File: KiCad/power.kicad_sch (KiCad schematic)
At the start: 15 parts

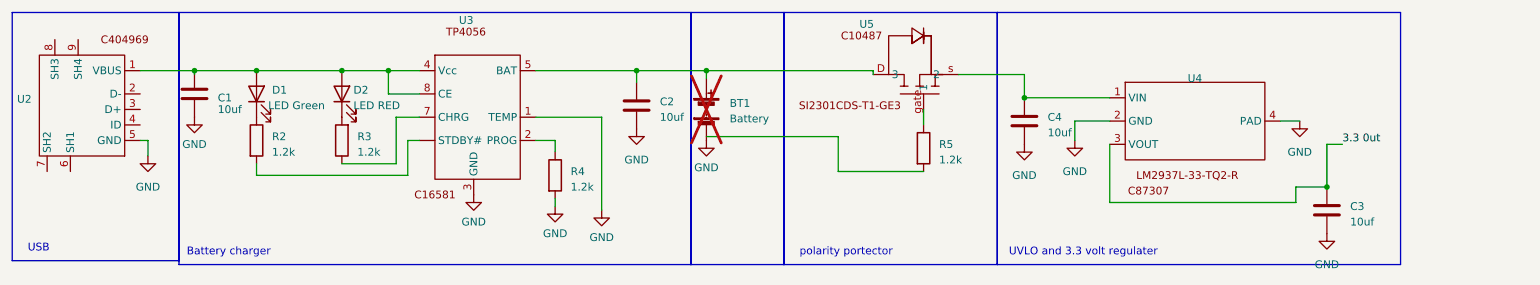
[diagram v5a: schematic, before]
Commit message: added heirachals and connected subsheets
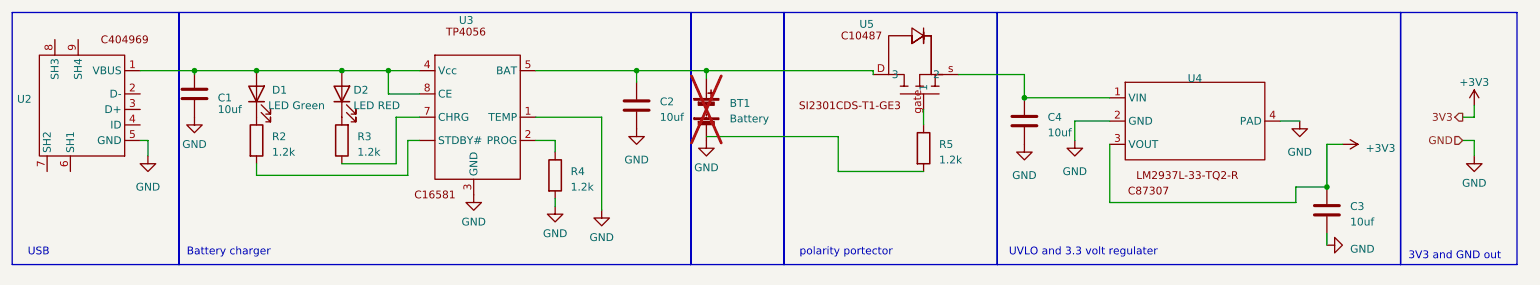
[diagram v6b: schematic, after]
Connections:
- net 3.3 0ut renamed +3V3
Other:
- note added: "3V3 and GND out"
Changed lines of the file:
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@@
+    (stroke (width 0) (type default))
+  )
+  (wire (pts (xy 262.89 38.1) (xy 260.985 38.1))
     (stroke (width 0) (type default))
   )
@@
     (stroke (width 0) (type default))
   )
+  (wire (pts (xy 262.89 36.195) (xy 262.89 38.1))
+    (stroke (width 0) (type default))
+  )
   (wire (pts (xy 189.23 31.115) (xy 189.23 34.925))
     (stroke (width 0) (type default))
@@
     (stroke (width 0) (type default))
   )
+  (wire (pts (xy 260.985 41.91) (xy 262.89 41.91))
+    (stroke (width 0) (type default))
+  )
+  (wire (pts (xy 262.89 41.91) (xy 262.89 44.45))
+    (stroke (width 0) (type default))
+  )
   (wire (pts (xy 63.5 30.48) (xy 77.47 30.48))
     (stroke (width 0) (type default))
@@
     (stroke (width 0) (type default))
   )
+  (wire (pts (xy 238.76 57.15) (xy 238.76 59.055))
+    (stroke (width 0) (type default))
+  )
   (wire (pts (xy 86.36 45.72) (xy 86.36 38.1))
     (stroke (width 0) (type default))
@@
     (fill (type none))
   )
-  (rectangle (start 23.495 20.955) (end 50.8 61.595)
+  (rectangle (start 23.495 20.955) (end 50.8 62.23)
+    (stroke (width 0) (type default))
+    (fill (type none))
+  )
+  (rectangle (start 250.825 20.955) (end 269.875 62.23)
     (stroke (width 0) (type default))
     (fill (type none))
@@
     (effects (font (size 1.27 1.27)) (justify left bottom))
   )
+  (text "3V3 and GND out\n" (at 252.095 61.595 0)
+    (effects (font (size 1.27 1.27)) (justify left bottom))
+  )
   (text "Battery charger " (at 52.07 60.96 0)
     (effects (font (size 1.27 1.27)) (justify left bottom))
   )
-  (text "USB" (at 26.035 60.325 0)
+  (text "USB" (at 26.035 60.96 0)
     (effects (font (size 1.27 1.27)) (justify left bottom))
   )
@@
     (effects (font (size 1.27 1.27)) (justify left bottom))
   )
-  (label "3.3 0ut" (at 241.3 42.545 0) (fields_autoplaced)
-    (effects (font (size 1.27 1.27)) (justify left bottom))
+  (hierarchical_label "GND" (shape input) (at 260.985 41.91 180) (fields_autoplaced)
+    (effects (font (size 1.27 1.27)) (justify right))
+  )
+  (hierarchical_label "3V3" (shape output) (at 260.985 38.1 180) (fields_autoplaced)
+    (effects (font (size 1.27 1.27)) (justify right))
+  )
+  (symbol (lib_id "power:+3V3") (at 241.3 42.545 270) (unit 1)
+    (in_bom yes) (on_board yes) (dnp no) (fields_autoplaced)
+    (property "Reference" "#PWR040" (at 237.49 42.545 0)
+      (effects (font (size 1.27 1.27)) hide)
+    )
+    (property "Value" "+3V3" (at 245.11 43.18 90)
+      (effects (font (size 1.27 1.27)) (justify left))
+    )
+    (property "Footprint" "" (at 241.3 42.545 0)
+      (effects (font (size 1.27 1.27)) hide)
+    )
+    (property "Datasheet" "" (at 241.3 42.545 0)
+      (effects (font (size 1.27 1.27)) hide)
+    )
+    (pin "1")
+    (instances
+      (project "EEE3088F_CKR"
+        (path "/31e5d740-f3fb-4029-be8d-dfdc4f653d72/d53a003e-af2e-46c6-8ee9-c5701cef8adb"
+          (reference "#PWR040") (unit 1)
+        )
+      )
+    )
   )
   (symbol (lib_id "Device:LED") (at 77.47 34.29 90) (unit 1)
@@
     )
   )
+  (symbol (lib_id "power:+3V3") (at 262.89 36.195 0) (unit 1)
+    (in_bom yes) (on_board yes) (dnp no) (fields_autoplaced)
+    (property "Reference" "#PWR041" (at 262.89 40.005 0)
+      (effects (font (size 1.27 1.27)) hide)
+    )
+    (property "Value" "+3V3" (at 262.89 32.385 0)
+      (effects (font (size 1.27 1.27)))
+    )
+    (property "Footprint" "" (at 262.89 36.195 0)
+      (effects (font (size 1.27 1.27)) hide)
+    )
+    (property "Datasheet" "" (at 262.89 36.195 0)
+      (effects (font (size 1.27 1.27)) hide)
+    )
+    (pin "1")
+    (instances
+      (project "EEE3088F_CKR"
+        (path "/31e5d740-f3fb-4029-be8d-dfdc4f653d72/d53a003e-af2e-46c6-8ee9-c5701cef8adb"
+          (reference "#PWR041") (unit 1)
+        )
+      )
+    )
+  )
   (symbol (lib_id "Device:R") (at 172.72 43.18 0) (unit 1)
     (in_bom yes) (on_board yes) (dnp no) (fields_autoplaced)
@@
     )
   )
-  (symbol (lib_id "power:GND") (at 238.76 57.15 0) (unit 1)
-    (in_bom yes) (on_board yes) (dnp no) (fields_autoplaced)
-    (property "Reference" "#PWR015" (at 238.76 63.5 0)
-      (effects (font (size 1.27 1.27)) hide)
-    )
-    (property "Value" "GND" (at 238.76 62.23 0)
-      (effects (font (size 1.27 1.27)))
-    )
-    (property "Footprint" "" (at 238.76 57.15 0)
-      (effects (font (size 1.27 1.27)) hide)
-    )
-    (property "Datasheet" "" (at 238.76 57.15 0)
+  (symbol (lib_id "power:GND") (at 238.76 59.055 90) (unit 1)
+    (in_bom yes) (on_board yes) (dnp no) (fields_autoplaced)
+    (property "Reference" "#PWR015" (at 245.11 59.055 0)
+      (effects (font (size 1.27 1.27)) hide)
+    )
+    (property "Value" "GND" (at 242.57 59.69 90)
+      (effects (font (size 1.27 1.27)) (justify right))
+    )
+    (property "Footprint" "" (at 238.76 59.055 0)
+      (effects (font (size 1.27 1.27)) hide)
+    )
+    (property "Datasheet" "" (at 238.76 59.055 0)
       (effects (font (size 1.27 1.27)) hide)
     )
@@
         )
       )
+    )
+  )
+  (symbol (lib_id "power:GND") (at 262.89 44.45 0) (unit 1)
+    (in_bom yes) (on_board yes) (dnp no) (fields_autoplaced)
+    (property "Reference" "#PWR042" (at 262.89 50.8 0)
+      (effects (font (size 1.27 1.27)) hide)
+    )
+    (property "Value" "GND" (at 262.89 48.895 0)
+      (effects (font (size 1.27 1.27)))
+    )
+    (property "Footprint" "" (at 262.89 44.45 0)
+      (effects (font (size 1.27 1.27)) hide)
+    )
+    (property "Datasheet" "" (at 262.89 44.45 0)
+      (effects (font (size 1.27 1.27)) hide)
+    )
+    (pin "1")
+    (instances
+      (project "EEE3088F_CKR"
+        (path "/31e5d740-f3fb-4029-be8d-dfdc4f653d72/d53a003e-af2e-46c6-8ee9-c5701cef8adb"
+          (reference "#PWR042") (unit 1)
+        )
+      )
+      (project "power"
+        (path "/d9c34bc1-cf5e-42ef-a2b2-2cfbae723006"
+          (reference "#PWR015") (unit 1)
+        )
+      )
